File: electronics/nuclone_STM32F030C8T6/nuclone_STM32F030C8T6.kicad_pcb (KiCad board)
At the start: 2 copper layers, 48.2 x 76.2 mm, 39 parts, among them J1 JTAG_2X05, J2 TYPE-C-31-M-12, J3 nuclone_medium_left, J4 nuclone_medium_right, SW1 RESET, SW2 Bootloader, U1 MCP1702-MB

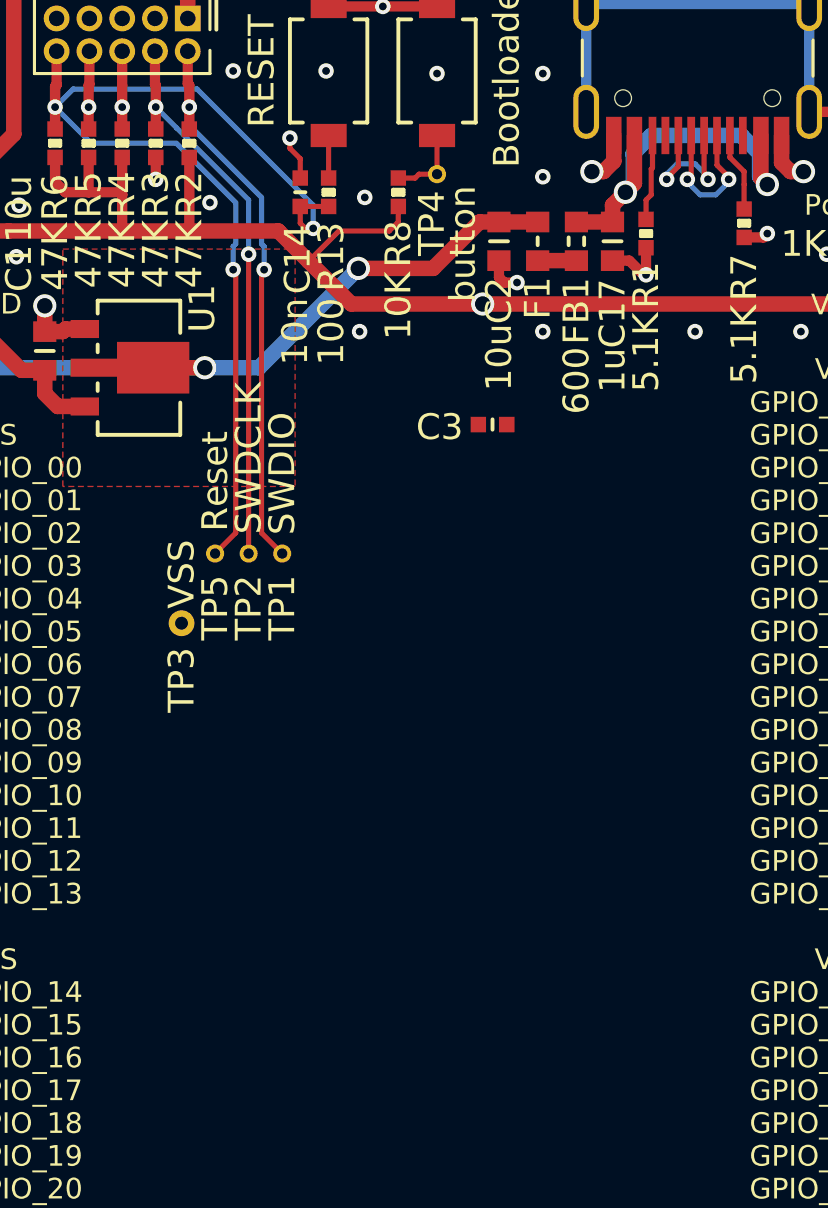
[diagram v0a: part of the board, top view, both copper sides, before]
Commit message: schematic and inital placement in progress
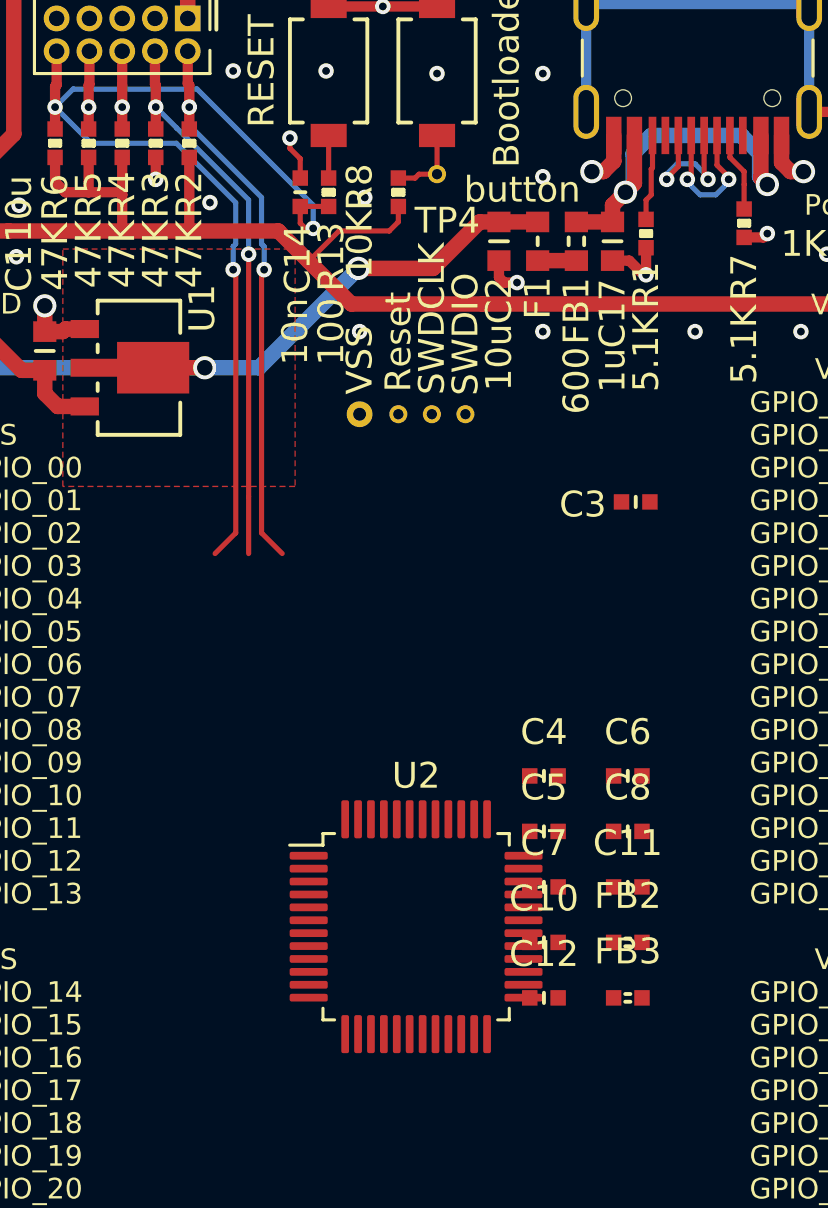
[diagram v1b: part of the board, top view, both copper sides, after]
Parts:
- added C10: 10n, SquantorRcl:C_0402, F.Cu at (90.0, 99.7)
- added C11: 10n, SquantorRcl:C_0402, F.Cu at (93.3, 97.5)
- added C12: 10n, SquantorRcl:C_0402, F.Cu at (90.0, 101.8)
- added C4: 100n, SquantorRcl:C_0402, F.Cu at (90.0, 93.2)
- added C5: 100n, SquantorRcl:C_0402, F.Cu at (90.0, 95.4)
- added C6: 100n, SquantorRcl:C_0402, F.Cu at (93.3, 93.2)
- added C7: 10n, SquantorRcl:C_0402, F.Cu at (90.0, 97.5)
- added C8: 100n, SquantorRcl:C_0402, F.Cu at (93.3, 95.4)
- added FB2: 600, SquantorRcl:L_0402, F.Cu at (93.3, 99.7)
- added FB3: 600, SquantorRcl:L_0402, F.Cu at (93.3, 101.8)
- added U2: STM32F030C8T6, Package_QFP:LQFP-48_7x7mm_P0.5mm, F.Cu at (85.1, 99.1)
- moved TP3 10.6 mm to (82.9, 79.2)
- moved TP2 8.92 mm to (85.7, 79.2)
- moved TP5 8.92 mm to (84.4, 79.2)
- moved TP1 8.92 mm to (87.0, 79.2)
- moved C3 6.31 mm to (93.6, 82.6)
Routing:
- net /VDD: track 90.2 -> 90.1 mm, vias 1 -> 0

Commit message: adding jumpers and some additional layout
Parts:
- added JP1: PA13, SquantorSpecial:solder_jumper_2way_noconn, B.Cu at (89.9, 101.3)
- added JP2: PA14, SquantorSpecial:solder_jumper_2way_noconn, B.Cu at (89.9, 99.0)
- added JP3: PC14/OSC32, SquantorSpecial:solder_jumper_3way_12conn, B.Cu at (81.8, 101.3)
- added JP4: PC15/OSC32, SquantorSpecial:solder_jumper_3way_12conn, B.Cu at (81.8, 99.0)
- added JP5: PF0/OSC, SquantorSpecial:solder_jumper_3way_12conn, B.Cu at (86.2, 101.3)
- added JP6: PF1/OSC, SquantorSpecial:solder_jumper_3way_12conn, B.Cu at (86.2, 99.0)
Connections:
- U2 pad 3: /GPIO_01 -> /microcontroller/OSC32IN_MCU
- U2 pad 34: /GPIO_39 -> /TMS
- U2 pad 37: /GPIO_42 -> /TCK
- U2 pad 4: /GPIO_02 -> /microcontroller/OSC32OUT_MCU
- U2 pad 5: /GPIO_03 -> /microcontroller/OSCIN_MCU
- U2 pad 6: /GPIO_04 -> /microcontroller/OSCOUT_MCU

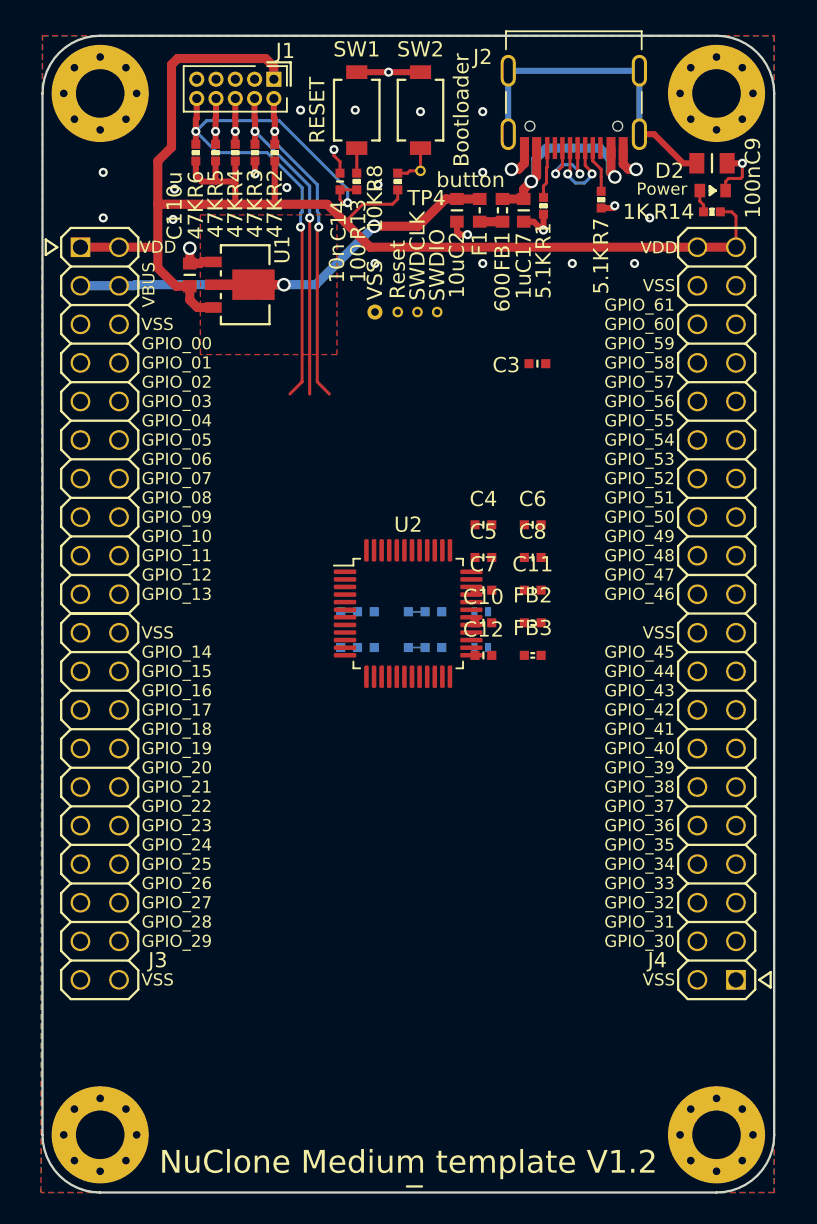
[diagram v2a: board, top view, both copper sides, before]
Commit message: updated stacked medium header
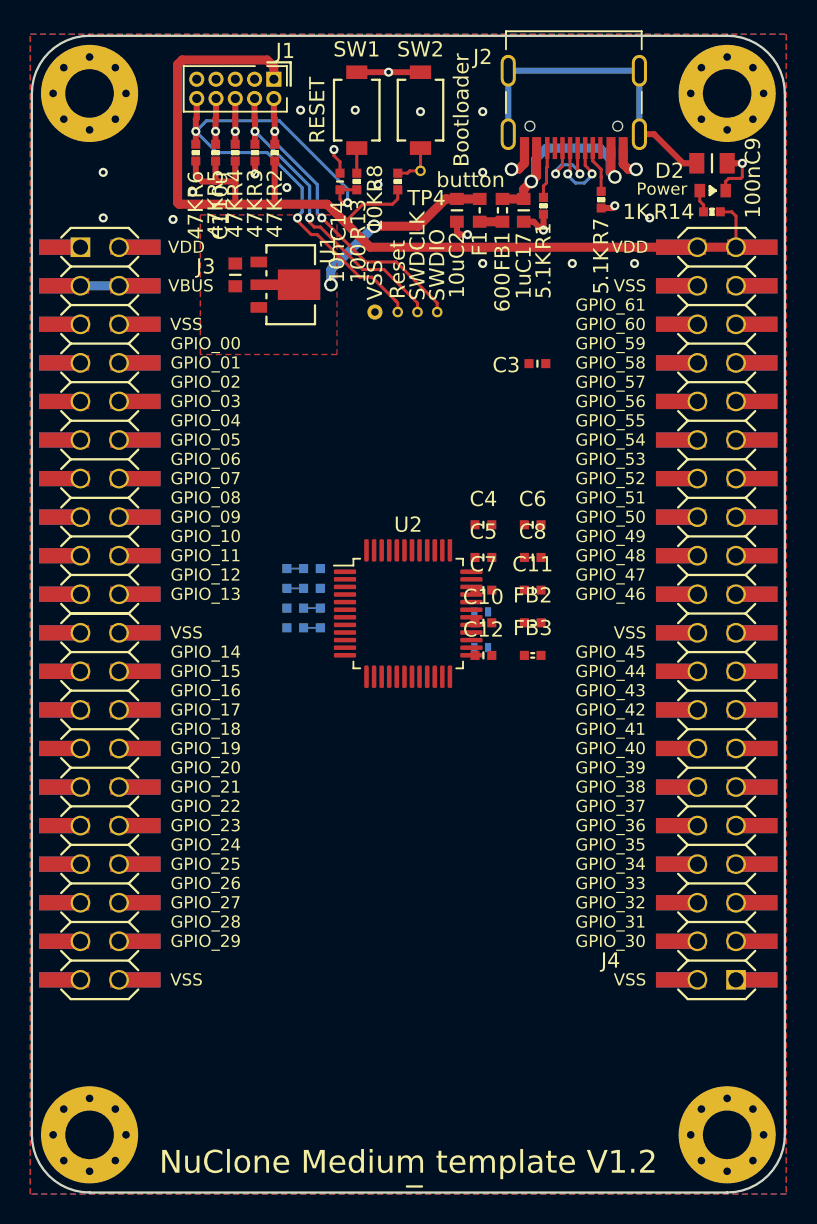
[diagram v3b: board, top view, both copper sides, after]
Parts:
- J3: footprint SquantorConnectorsNamed:nuclone_medium_left -> SquantorConnectorsNamed:nuclone_medium_left_stacked
- J4: footprint SquantorConnectorsNamed:nuclone_medium_right -> SquantorConnectorsNamed:nuclone_medium_right_stacked
- moved JP5 8.41 mm to (78.2, 98.7), turned to 180 degrees
- moved JP6 8.07 mm to (78.2, 100.0), turned to 180 degrees
- moved JP3 6.30 mm to (78.2, 96.1)
- moved JP4 3.87 mm to (78.2, 97.4)
- moved C1 3.00 mm to (73.7, 76.8)
- moved U1 3.00 mm to (77.0, 77.4)
- moved H1 0.70 mm to (64.1, 64.8)
- moved H4 0.70 mm to (64.1, 133.4)
- moved H2 0.70 mm to (106.1, 64.8)
- moved H3 0.70 mm to (106.1, 133.4)
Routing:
- net /VDD: track 90.1 -> 73.3 mm
- net /VBUS: track 32.4 -> 16.4 mm
- net /VSS: track 22.1 -> 19.5 mm, vias 26 -> 24
- net /RESET: track 41.0 -> 38.8 mm
- net /TCK: track 21.8 -> 20.4 mm
- net /TMS: track 21.9 -> 20.5 mm
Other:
- board size 48.2 x 76.2 mm -> 49.6 x 76.2 mm

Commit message: WIP STM32F030C8T6
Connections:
- J4 pad 10: /GPIO_37 -> /GPIO_36
- J4 pad 11: /GPIO_38 -> /GPIO_39
- J4 pad 12: /GPIO_39 -> /GPIO_38
- J4 pad 13: /GPIO_40 -> /GPIO_41
- J4 pad 14: /GPIO_41 -> /GPIO_40
- J4 pad 15: /GPIO_42 -> /GPIO_43
- J4 pad 16: /GPIO_43 -> /GPIO_42
- J4 pad 17: /GPIO_44 -> /GPIO_45
- J4 pad 18: /GPIO_45 -> /GPIO_44
- J4 pad 21: /GPIO_46 -> /GPIO_47
- J4 pad 22: /GPIO_47 -> /GPIO_46
- J4 pad 23: /GPIO_48 -> /GPIO_49
- J4 pad 24: /GPIO_49 -> /GPIO_48
- J4 pad 25: /GPIO_50 -> /GPIO_51
- J4 pad 26: /GPIO_51 -> /GPIO_50
- J4 pad 27: /GPIO_52 -> /GPIO_53
- J4 pad 28: /GPIO_53 -> /GPIO_52
- J4 pad 29: /GPIO_54 -> /GPIO_55
- J4 pad 3: /GPIO_30 -> /GPIO_31
- J4 pad 30: /GPIO_55 -> /GPIO_54
- J4 pad 31: /GPIO_56 -> /GPIO_57
- J4 pad 32: /GPIO_57 -> /GPIO_56
- J4 pad 33: /GPIO_58 -> /GPIO_59
- J4 pad 34: /GPIO_59 -> /GPIO_58
- J4 pad 35: /GPIO_60 -> /GPIO_61
- J4 pad 36: /GPIO_61 -> /GPIO_60
- J4 pad 4: /GPIO_31 -> /GPIO_30
- J4 pad 5: /GPIO_32 -> /GPIO_33
- J4 pad 6: /GPIO_33 -> /GPIO_32
- J4 pad 7: /GPIO_34 -> /GPIO_35
- J4 pad 8: /GPIO_35 -> /GPIO_34
- J4 pad 9: /GPIO_36 -> /GPIO_37
- JP1 pad 1: /GPIO_39 -> /GPIO_50
- JP2 pad 1: /GPIO_42 -> /GPIO_53
- U2 pad 25: /GPIO_30 -> /GPIO_41
- U2 pad 26: /GPIO_31 -> /GPIO_42
- U2 pad 27: /GPIO_32 -> /GPIO_43
- U2 pad 28: /GPIO_33 -> /GPIO_44
- U2 pad 29: /GPIO_34 -> /GPIO_45
- U2 pad 30: /GPIO_35 -> /GPIO_46
- U2 pad 31: /GPIO_36 -> /GPIO_47
- U2 pad 32: /GPIO_37 -> /GPIO_48
- U2 pad 33: /GPIO_38 -> /GPIO_49
- U2 pad 35: /GPIO_40 -> /GPIO_51
- U2 pad 36: /GPIO_41 -> /GPIO_52
- U2 pad 38: /GPIO_43 -> /GPIO_54
- U2 pad 39: /GPIO_44 -> /GPIO_55
- U2 pad 40: /GPIO_45 -> /GPIO_56
- U2 pad 41: /GPIO_46 -> /GPIO_57
- U2 pad 42: /GPIO_47 -> /GPIO_58
- U2 pad 43: /GPIO_48 -> /GPIO_59
- U2 pad 45: /GPIO_49 -> /GPIO_60
- U2 pad 46: /GPIO_50 -> /GPIO_61
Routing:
- net /VSS: vias 24 -> 23

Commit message: matching board with template
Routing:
- net /VDD: track 73.3 -> 92.3 mm
- net /VBUS: track 16.4 -> 29.3 mm
- net /RESET: track 38.8 -> 31.3 mm
- net /VSS: track 19.5 -> 22.6 mm, vias 23 -> 24

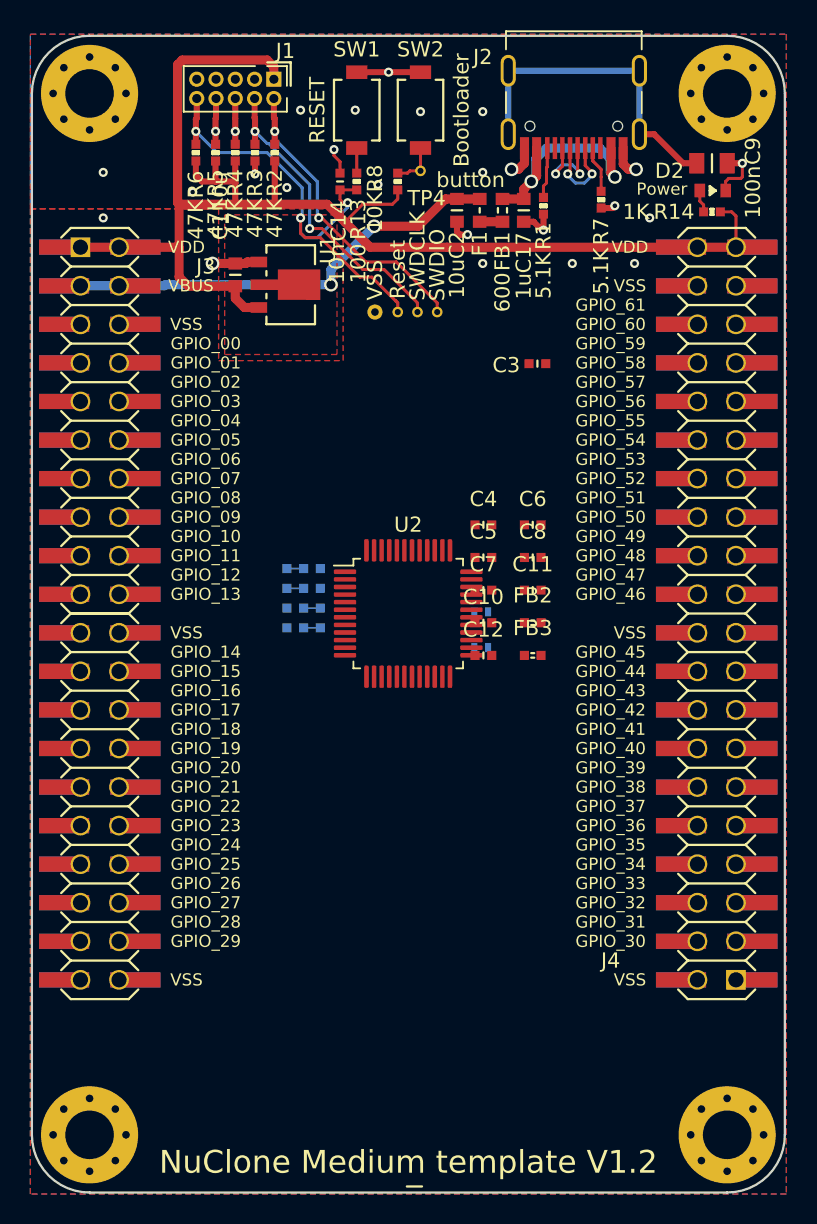
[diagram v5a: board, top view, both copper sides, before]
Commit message: added crystals to board
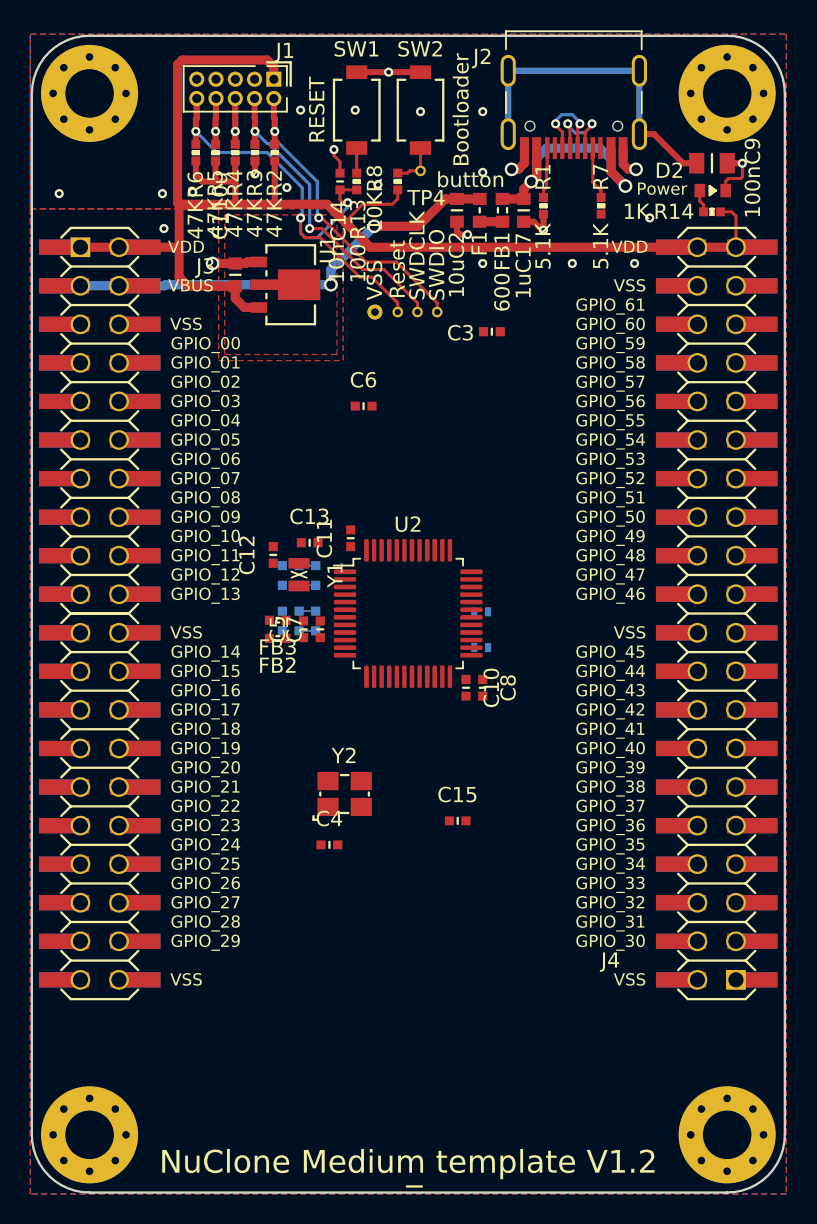
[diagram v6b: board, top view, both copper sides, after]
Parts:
- added C13: 10p, SquantorRcl:C_0402, F.Cu at (78.6, 94.4)
- added C15: 10p, SquantorRcl:C_0402, F.Cu at (88.3, 112.7)
- added Y1: 32KHz, SquantorCrystal:Crystal_2012_2, F.Cu at (77.9, 96.5)
- added Y2: 16MHz, SquantorCrystal:Crystal_3225_4, F.Cu at (80.9, 111.0)
- C12: value 10n -> 10p
- C4: value 100n -> 10p
- moved C4 23.4 mm to (79.9, 114.3)
- moved FB3 17.0 mm to (76.5, 99.5), turned to 180 degrees
- moved FB2 16.8 mm to (76.5, 100.7), turned to 180 degrees
- moved C12 15.3 mm to (76.2, 95.2), turned to 90 degrees
- moved C6 13.6 mm to (82.2, 85.4)
- moved C5 12.8 mm to (78.2, 100.1), turned to 90 degrees
- moved C11 12.5 mm to (81.3, 94.1), turned to 90 degrees
- moved C7 11.0 mm to (79.3, 100.1), turned to 90 degrees
- moved C8 9.19 mm to (90.0, 104.0), turned to 270 degrees
- moved C10 4.43 mm to (88.9, 104.0), turned to 270 degrees
- moved C3 3.66 mm to (90.6, 80.5)
- moved R7 0.40 mm to (97.8, 72.2)
- moved JP4 0.36 mm to (77.9, 97.2), turned to 180 degrees
- moved JP5 0.36 mm to (77.9, 98.9)
- moved JP6 0.36 mm to (77.9, 100.2)
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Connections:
- C12 pad 1: /VDD -> /VSS
- C12 pad 2: /VSS -> /microcontroller/OSC32IN
- C4 pad 1: /VDD -> /VSS
- C4 pad 2: /VSS -> /microcontroller/OSCIN
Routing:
- net Net-(C17-Pad2): track 15.5 -> 17.3 mm
- net /VSS: track 22.6 -> 21.7 mm
- net Net-(J2-PadA5): track 3.08 -> 3.88 mm

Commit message: further routing and placing of parts
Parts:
- moved C4 18.6 mm to (73.9, 96.7), turned to 270 degrees
- moved C15 18.5 mm to (79.1, 96.7), turned to 90 degrees
- moved Y2 14.9 mm to (76.5, 96.7)
- moved C6 8.92 mm to (80.2, 94.1), turned to 90 degrees
- moved JP4 5.41 mm to (76.8, 91.9), turned to 90 degrees
- moved C12 4.85 mm to (78.0, 90.7), turned to 270 degrees
- moved JP2 4.65 mm to (87.8, 94.8), turned to 270 degrees
- moved C13 4.07 mm to (76.9, 90.7), turned to 90 degrees
- moved JP1 4.05 mm to (89.2, 97.3), turned to 180 degrees
- moved JP3 4.00 mm to (78.1, 91.9), turned to 90 degrees
- moved Y1 3.83 mm to (77.5, 92.7), turned to 180 degrees
- moved JP5 3.36 mm to (76.2, 96.0)
- moved JP6 3.36 mm to (76.2, 97.3)
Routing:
- net /VDD: track 92.3 -> 130.6 mm, vias 0 -> 3
- net /GPIO_06: track 0.00 -> 32.3 mm, vias 0 -> 2
- net /GPIO_61: track 0.00 -> 32.3 mm
- net /Bootloader: track 3.06 -> 35.0 mm, vias 0 -> 4
- net /GPIO_00: track 0.00 -> 31.6 mm, vias 0 -> 2
- net /GPIO_12: track 0.00 -> 30.0 mm
- net /GPIO_59: track 0.00 -> 29.8 mm
- net /GPIO_10: track 0.00 -> 29.6 mm
- net /GPIO_08: track 0.00 -> 29.4 mm
- net /GPIO_16: track 0.00 -> 28.8 mm
- net /GPIO_14: track 0.00 -> 27.9 mm
- net /GPIO_05: track 0.00 -> 27.6 mm, vias 0 -> 2
- net /GPIO_57: track 0.00 -> 27.6 mm
- net /GPIO_60: track 0.00 -> 27.0 mm
- net /GPIO_07: track 0.00 -> 26.3 mm, vias 0 -> 2
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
